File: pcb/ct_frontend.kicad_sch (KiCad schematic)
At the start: 5 parts, among them J1 SJ-3524-SMT-TR

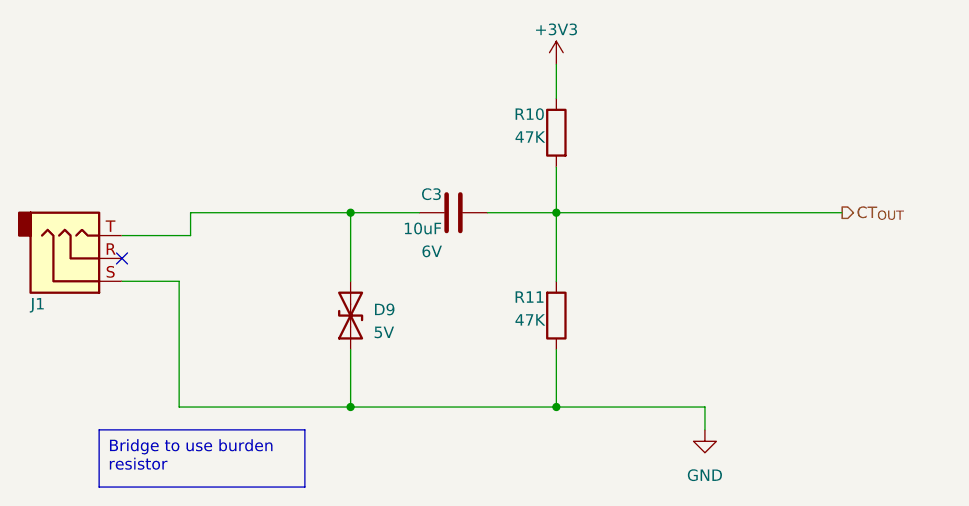
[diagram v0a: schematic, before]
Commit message: * Work in progress
  - Add generate script
  - Add switch model
  - Start routing
  - Tidy schematic
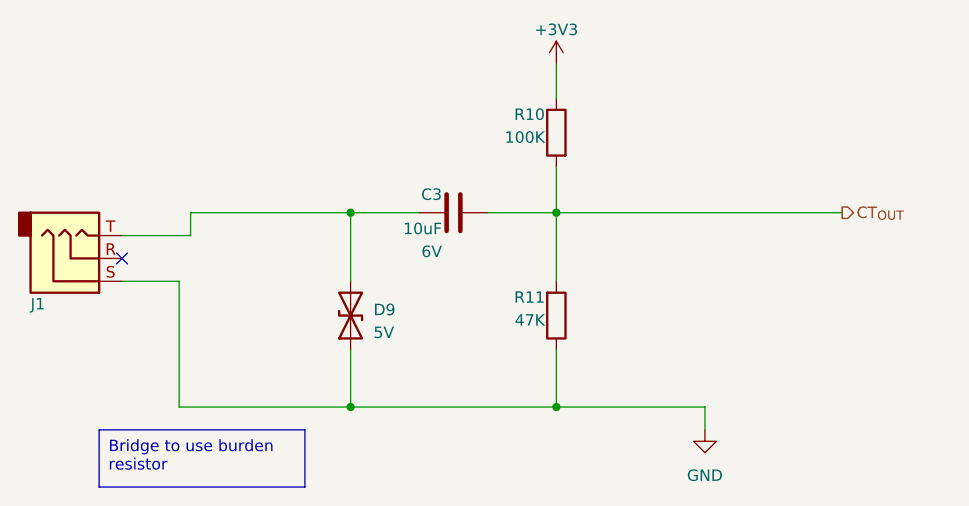
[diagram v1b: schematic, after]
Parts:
- R10: value 47K -> 100K
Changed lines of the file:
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@@
       (effects (font (size 1.27 1.27)) (justify left bottom))
     )
-    (property "Value" "47K" (at 149.86 77.47 0)
+    (property "Value" "100K" (at 149.86 77.47 0)
       (effects (font (size 1.27 1.27)) (justify left bottom))
     )
